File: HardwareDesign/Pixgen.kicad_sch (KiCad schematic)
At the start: 10 parts, among them U601 GAL22V10, U602 74HCT574, U603 27SF512, U604 74HCT574, U605 GAL22V10

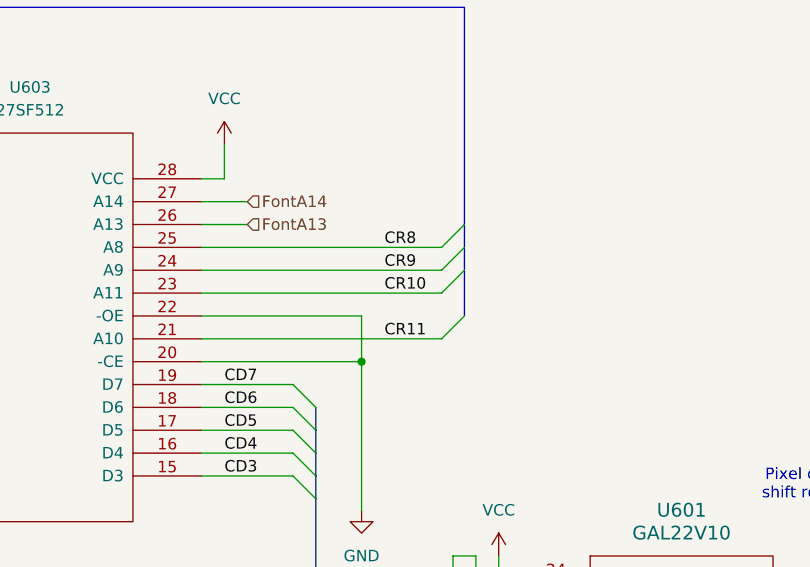
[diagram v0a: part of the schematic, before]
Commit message: fixed some mistakes in Pixgen module
Some of the character row address labels on nets
going to the character ROM were wrong.
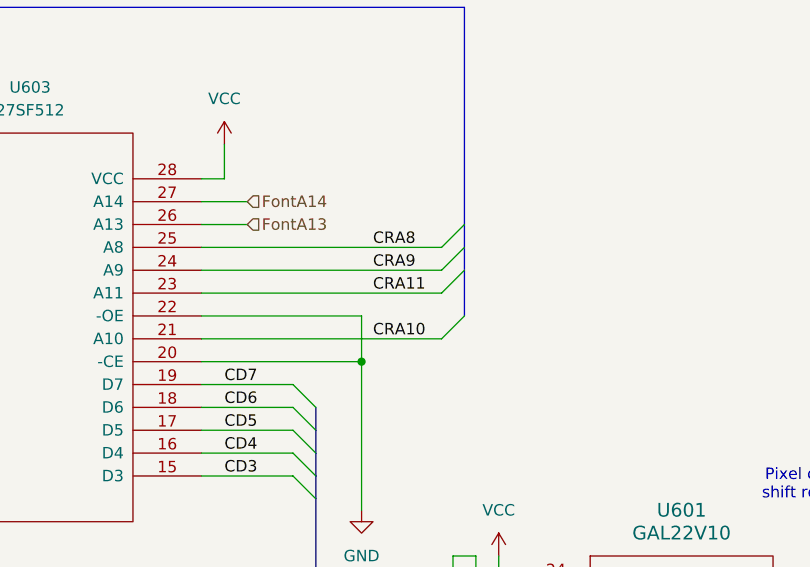
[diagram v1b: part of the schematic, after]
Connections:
- net CR10 is gone; now on net VC3: U603.23 (A11)
- net CR11 is gone; now on net VC2: U603.21 (A10)
- net CR8 is gone; now on net VC0: U603.25 (A8)
- net CR9 is gone; now on net VC1: U603.24 (A9)
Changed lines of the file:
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@@
 		)
 	)
-	(label "CR11"
-		(at 194.31 57.15 0)
+	(label "CRA11"
+		(at 193.04 52.07 0)
 		(fields_autoplaced yes)
 		(effects
@@
 		)
 	)
-	(label "CR10"
-		(at 194.31 52.07 0)
+	(label "CRA10"
+		(at 193.04 57.15 0)
 		(fields_autoplaced yes)
 		(effects
@@
 		)
 	)
-	(label "CR8"
-		(at 194.31 46.99 0)
+	(label "CRA8"
+		(at 193.04 46.99 0)
 		(fields_autoplaced yes)
 		(effects
@@
 		)
 	)
-	(label "CR9"
-		(at 194.31 49.53 0)
-		(fields_autoplaced yes)
-		(effects
+	(label "CRA9"
+		(at 193.04 49.53 0)
+		(fields_autoplaced yes)
+		(effects

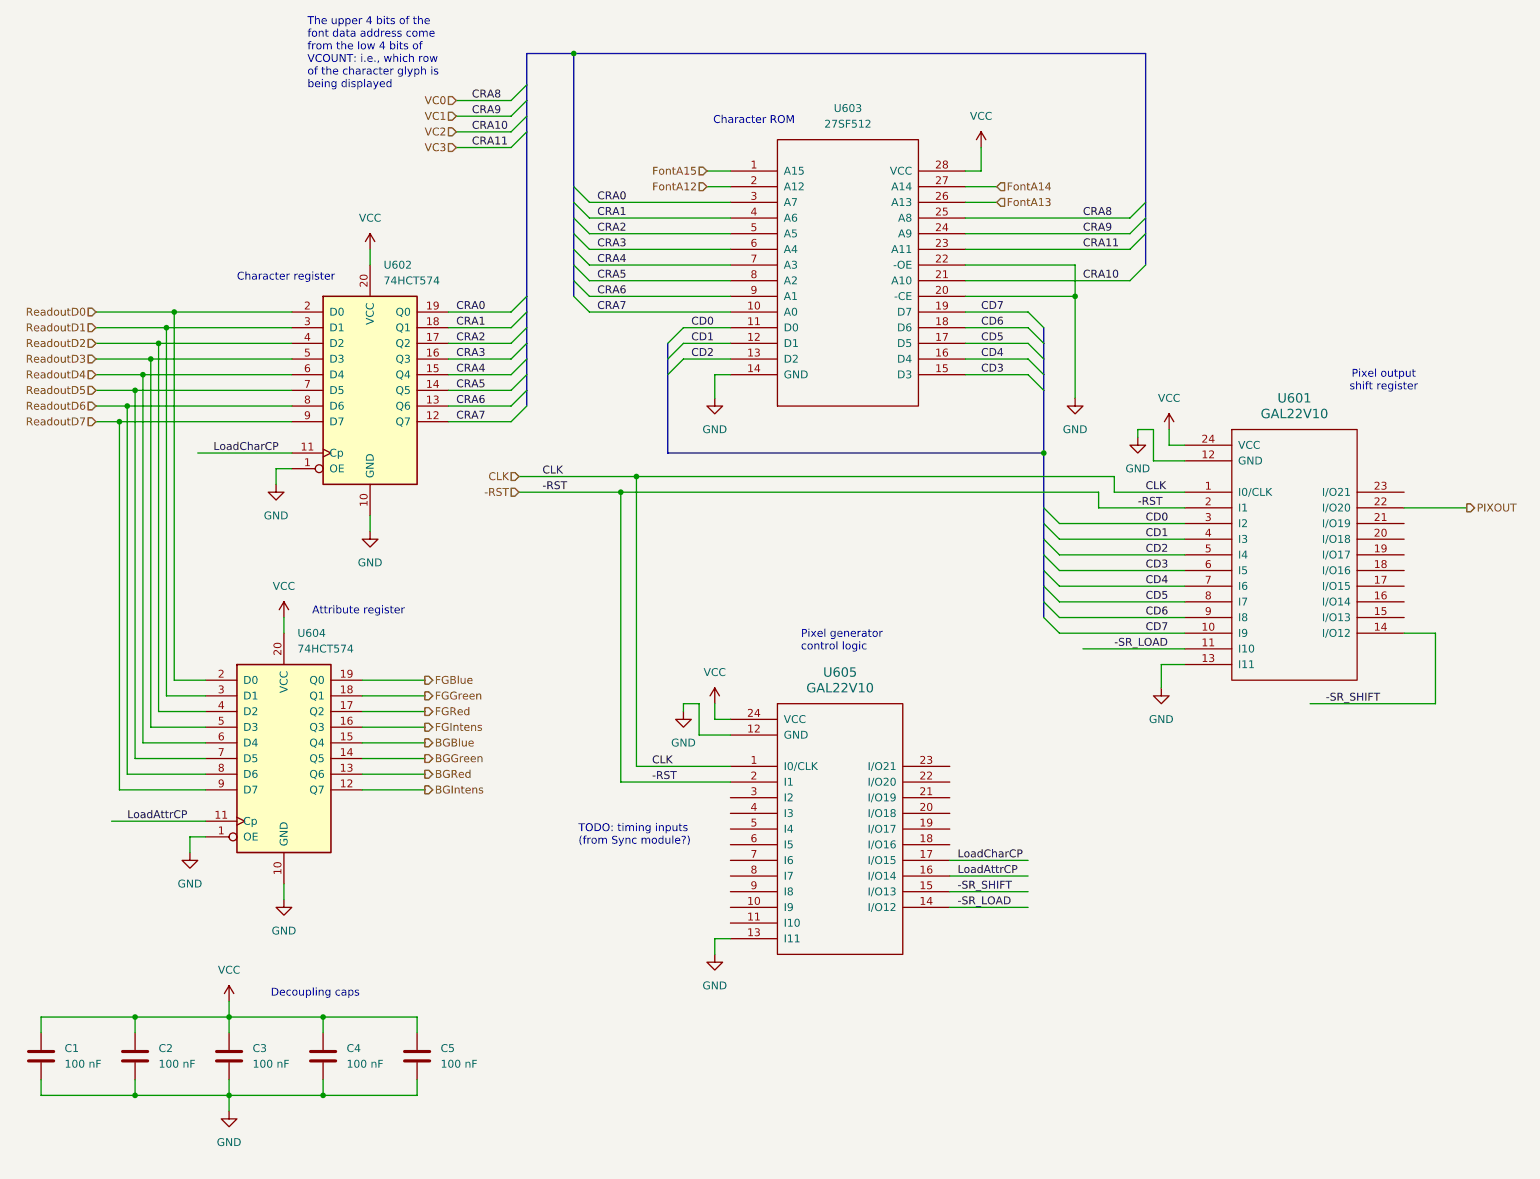
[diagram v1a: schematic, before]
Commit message: much work on pixel generation schematic, logic
In theory, this is potentially a complete hardware design,
but need to simulate it to make sure it will actually work.
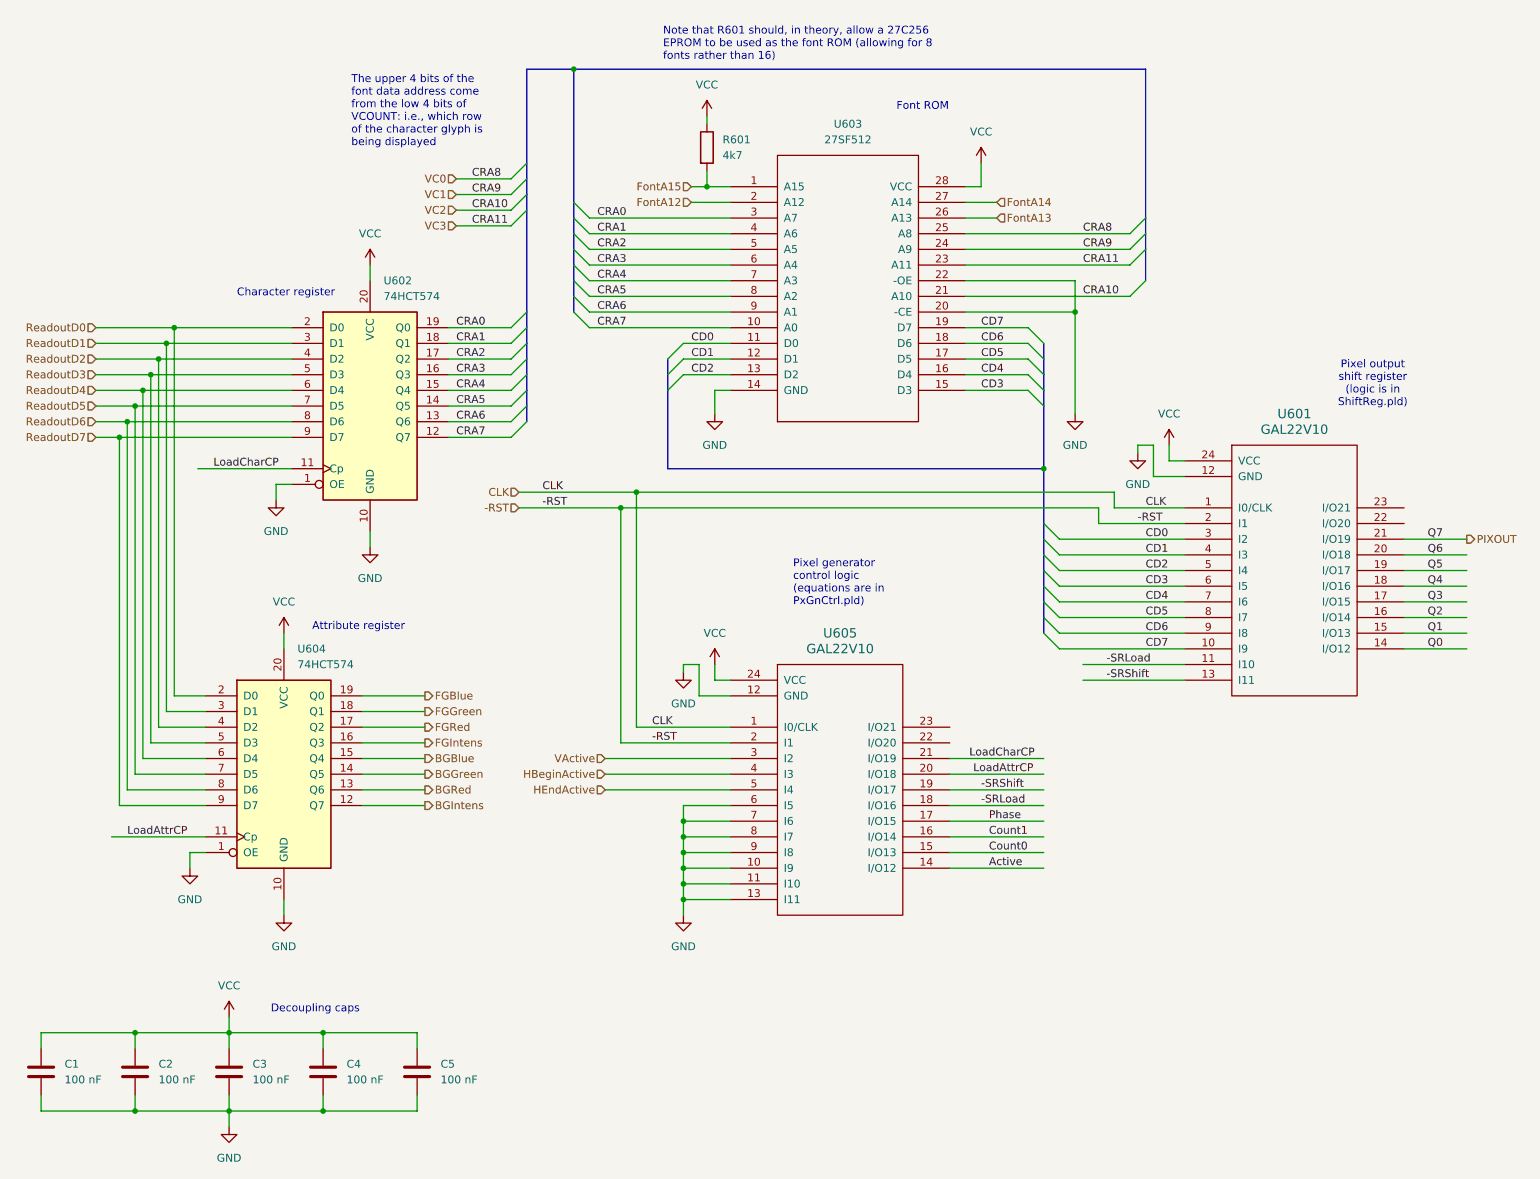
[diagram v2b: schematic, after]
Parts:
- added R601: 4k7, symbol Device:R
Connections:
- net FontA15: now also R601.2
- net GND: now also U605.10 (I9), U605.11 (I10), U605.6 (I5), U605.7 (I6), U605.8 (I7), U605.9 (I8); no longer U601.13 (I11)
- net LoadAttrCP: now also U605.20 (I/O18); no longer U605.16 (I/O14)
- net LoadCharCP: now also U605.21 (I/O19); no longer U605.17 (I/O15)
- net PIXOUT: now also U601.21 (I/O19); no longer U601.22 (I/O20)
- net VCC: now also R601.1
- net Q1: now reaches U601.15 (I/O13)
- net Q2: now reaches U601.16 (I/O14)
- net Q3: now reaches U601.17 (I/O15)
- net Q4: now reaches U601.18 (I/O16)
- net Q5: now reaches U601.19 (I/O17)
- net Q6: now reaches U601.20 (I/O18)
- net -SRLoad: now reaches U605.18 (I/O16)
- net -SRLoad: now also U601.11 (I10)
- net -SRShift: now reaches U605.19 (I/O17)
- net -SRShift: now also U601.13 (I11)
- net VActive: now reaches U605.3 (I2)
- net HBeginActive: now reaches U605.4 (I3)
- net HEndActive: now reaches U605.5 (I4)
- net -SR_LOAD renamed Active
- net Active: no longer U601.11 (I10)
- net -SR_SHIFT renamed Count0
- net Count0: no longer U601.14 (I/O12)
- new net Count1: U605.16 (I/O14)
- new net Phase: U605.17 (I/O15)
- new net Q0: U601.14 (I/O12)
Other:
- note added: "Font ROM"
- note added: "Note that R601 should, in theory, allow a 27C256 EPROM to be used as the font ROM (allowing for 8 fonts rather than 16)"
- note added: "Pixel generator control logic (equations are in PxGnCtrl.pld)"
- note added: "Pixel output shift register (logic is in ShiftReg.pld)"
- note removed: "Character ROM"
- note removed: "Pixel generator control logic"
- note removed: "Pixel output shift register"
- note removed: "TODO: timing inputs (from Sync module?)"
- moved on the sheet: C1, C2, C3, C4, C5, U601, U602, U603, U604, U605

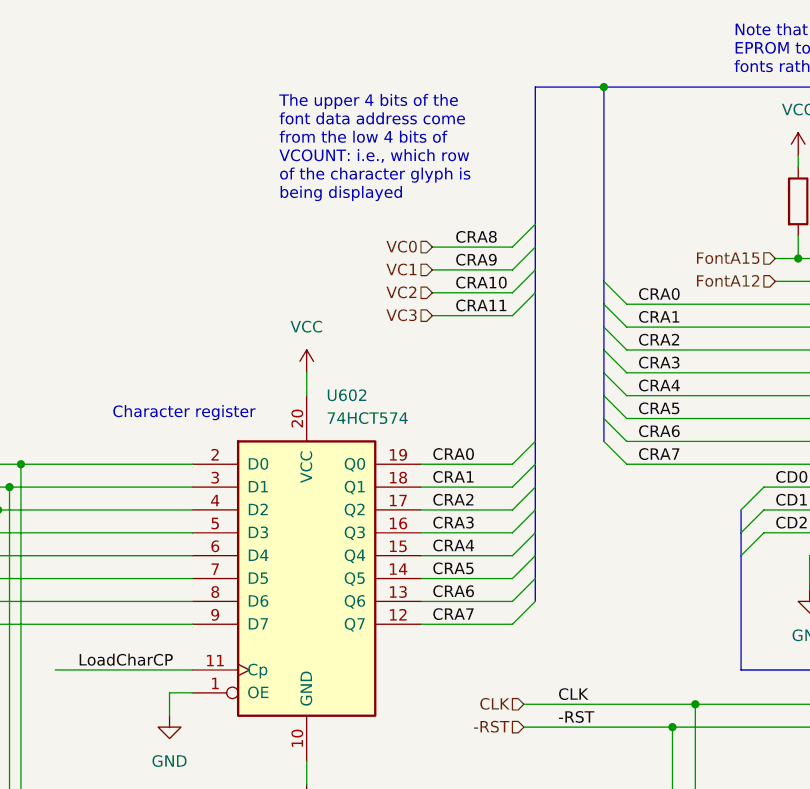
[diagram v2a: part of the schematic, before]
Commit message: map VCOUNT[3:0] to font address bits 3:0
Each character glyph in the font ROM is stored as 16
successive bytes representing pixel rows 0-15. Therefore,
VCOUNT[3:0] should drive the low 4 bits of the font
address.
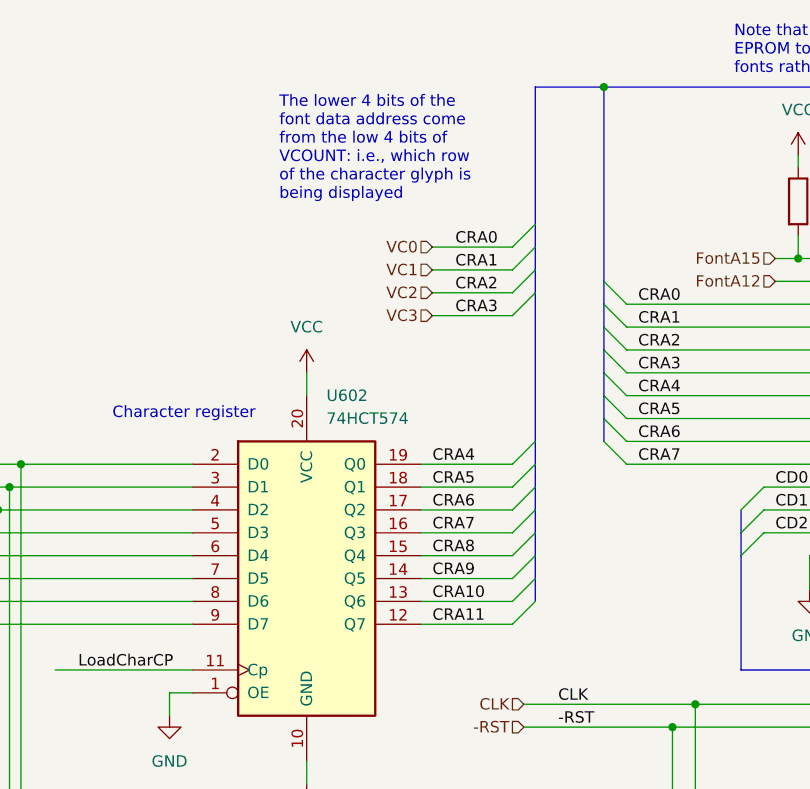
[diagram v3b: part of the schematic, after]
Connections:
- net CRA4: now also U602.19 (Q0); no longer U602.15 (Q4)
- net CRA5: now also U602.18 (Q1); no longer U602.14 (Q5)
- net CRA6: now also U602.17 (Q2); no longer U602.13 (Q6)
- net CRA7: now also U602.16 (Q3); no longer U602.12 (Q7)
- net VC0: now also U603.3 (A7); no longer U603.25 (A8)
- net VC1: now also U603.4 (A6); no longer U603.24 (A9)
- net VC2: now also U603.5 (A5); no longer U603.21 (A10)
- net VC3: now also U603.6 (A4); no longer U603.23 (A11)
- removed net CRA0: U602.19 (Q0), U603.3 (A7)
- removed net CRA1: U602.18 (Q1), U603.4 (A6)
- removed net CRA2: U602.17 (Q2), U603.5 (A5)
- removed net CRA3: U602.16 (Q3), U603.6 (A4)
- new net CRA10: U602.13 (Q6), U603.21 (A10)
- new net CRA11: U602.12 (Q7), U603.23 (A11)
- new net CRA8: U602.15 (Q4), U603.25 (A8)
- new net CRA9: U602.14 (Q5), U603.24 (A9)
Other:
- note added: "The lower 4 bits of the font data address come from the low 4 bits of VCOUNT: i.e., which row of the character glyph is being displayed"
- note removed: "The upper 4 bits of the font data address come from the low 4 bits of VCOUNT: i.e., which row of the character glyph is being displayed"
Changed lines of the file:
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@@
 		)
 	)
-	(text "The upper 4 bits of the\nfont data address come\nfrom the low 4 bits of\nVCOUNT: i.e., which row\nof the character glyph is\nbeing displayed"
+	(text "The lower 4 bits of the\nfont data address come\nfrom the low 4 bits of\nVCOUNT: i.e., which row\nof the character glyph is\nbeing displayed"
 		(exclude_from_sim no)
 		(at 74.422 29.718 0)
@@
 		)
 	)
-	(label "CRA11"
+	(label "CRA3"
 		(at 93.98 48.26 0)
 		(fields_autoplaced yes)
@@
 		)
 	)
-	(label "CRA9"
+	(label "CRA1"
 		(at 93.98 43.18 0)
 		(fields_autoplaced yes)
@@
 		)
 	)
-	(label "CRA8"
+	(label "CRA0"
 		(at 93.98 40.64 0)
 		(fields_autoplaced yes)
@@
 		)
 	)
-	(label "CRA10"
+	(label "CRA2"
 		(at 93.98 45.72 0)
 		(fields_autoplaced yes)
@@
 		)
 	)
-	(label "CRA3"
+	(label "CRA7"
 		(at 91.44 72.39 0)
 		(fields_autoplaced yes)
@@
 		)
 	)
-	(label "CRA2"
+	(label "CRA6"
 		(at 91.44 69.85 0)
 		(fields_autoplaced yes)
@@
 		)
 	)
-	(label "CRA0"
+	(label "CRA4"
 		(at 91.44 64.77 0)
 		(fields_autoplaced yes)
@@
 		)
 	)
-	(label "CRA5"
+	(label "CRA9"
 		(at 91.44 77.47 0)
 		(fields_autoplaced yes)
@@
 		)
 	)
-	(label "CRA4"
+	(label "CRA8"
 		(at 91.44 74.93 0)
 		(fields_autoplaced yes)
@@
 		)
 	)
-	(label "CRA1"
+	(label "CRA5"
 		(at 91.44 67.31 0)
 		(fields_autoplaced yes)
@@
 		)
 	)
-	(label "CRA7"
+	(label "CRA11"
 		(at 91.44 82.55 0)
 		(fields_autoplaced yes)
@@
 		)
 	)
-	(label "CRA6"
+	(label "CRA10"
 		(at 91.44 80.01 0)
 		(fields_autoplaced yes)

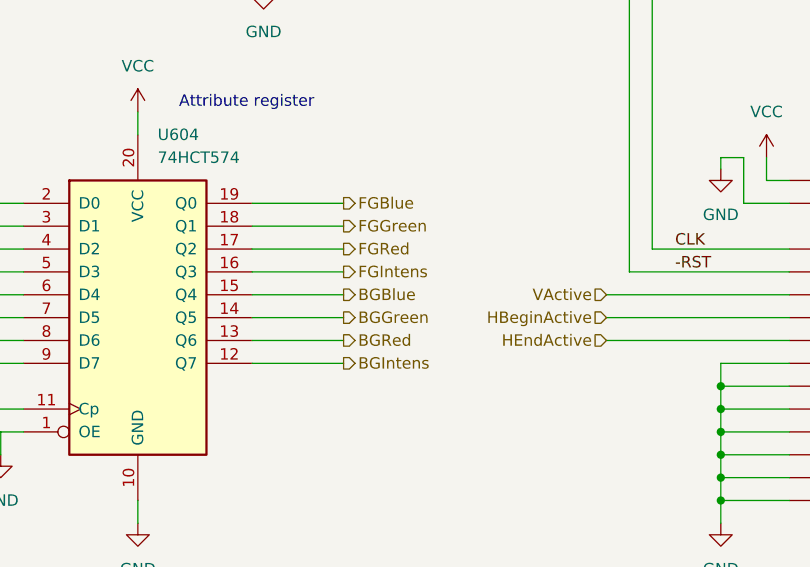
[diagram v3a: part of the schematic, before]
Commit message: high bits of attribute are fg, not bg
There's no particular reason, but this is how it's
documented in the Episode 03 video, so let's be
consistent.
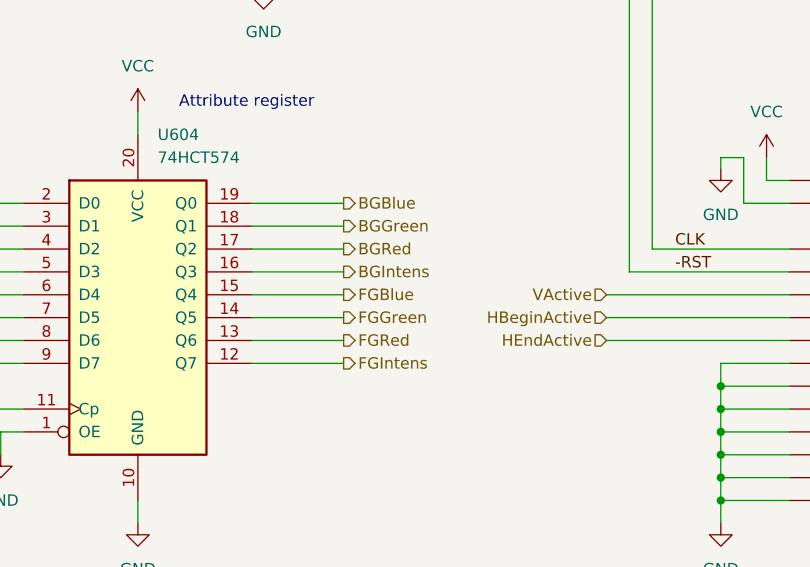
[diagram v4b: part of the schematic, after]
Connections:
- net BGBlue: now also U604.19 (Q0); no longer U604.15 (Q4)
- net BGGreen: now also U604.18 (Q1); no longer U604.14 (Q5)
- net BGIntens: now also U604.16 (Q3); no longer U604.12 (Q7)
- net BGRed: now also U604.17 (Q2); no longer U604.13 (Q6)
- net FGBlue: now also U604.15 (Q4); no longer U604.19 (Q0)
- net FGGreen: now also U604.14 (Q5); no longer U604.18 (Q1)
- net FGIntens: now also U604.12 (Q7); no longer U604.16 (Q3)
- net FGRed: now also U604.13 (Q6); no longer U604.17 (Q2)
